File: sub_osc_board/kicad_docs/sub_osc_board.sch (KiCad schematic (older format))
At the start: 25 parts, among them J1 signal_inputs, J2 pwm_inputs, J4 signal_outputs, J5 Conn_01x03, J6 Conn_01x03, J7 Conn_01x03, U10 TL072, U6 TL072, U9 TL072

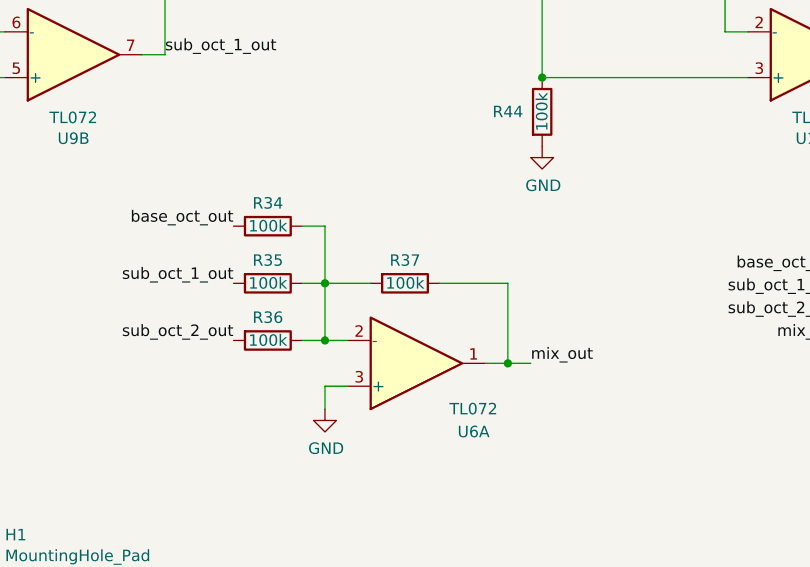
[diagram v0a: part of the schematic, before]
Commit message: change sub-osc PWM range and mixer gain
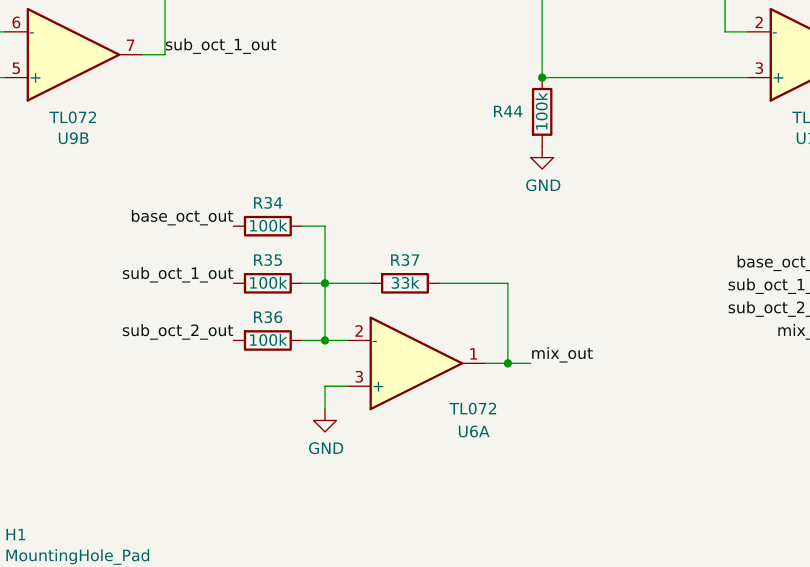
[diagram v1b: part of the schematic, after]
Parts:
- R37: value 100k -> 33k
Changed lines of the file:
@@
 P 7800 5600
 F 0 "R37" V 7700 5600 50  0000 C CNN
-F 1 "100k" V 7800 5600 50  0000 C CNN
+F 1 "33k" V 7800 5600 50  0000 C CNN
 F 2 "Resistor_SMD:R_0805_2012Metric_Pad1.15x1.40mm_HandSolder" V 7730 5600 50  0001 C CNN
 F 3 "~" H 7800 5600 50  0001 C CNN
